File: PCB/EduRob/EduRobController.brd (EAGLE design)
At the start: 75 x 53.5 mm, 31 parts, among them J1 665306124022, J2 665306124022, M3 665306124022, M4 665306124022

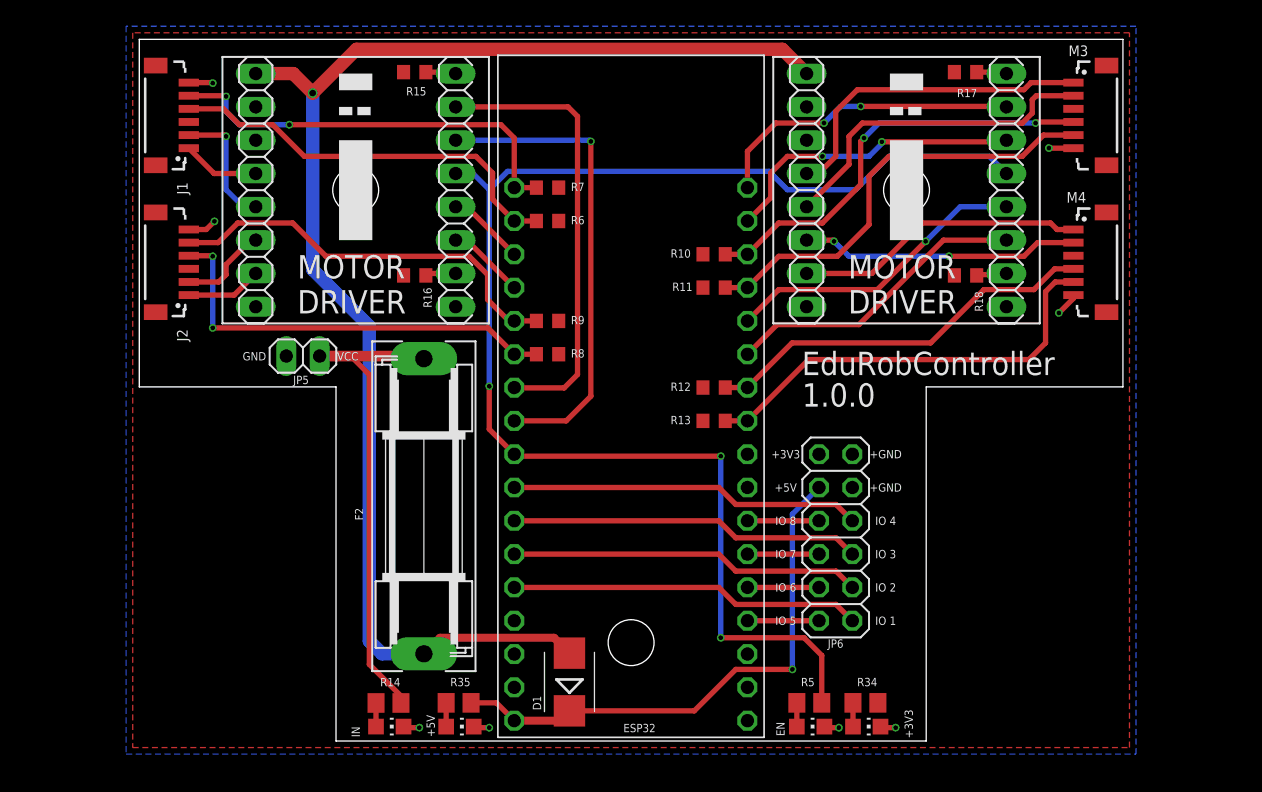
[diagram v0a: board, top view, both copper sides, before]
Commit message: New Connectors and minor changes
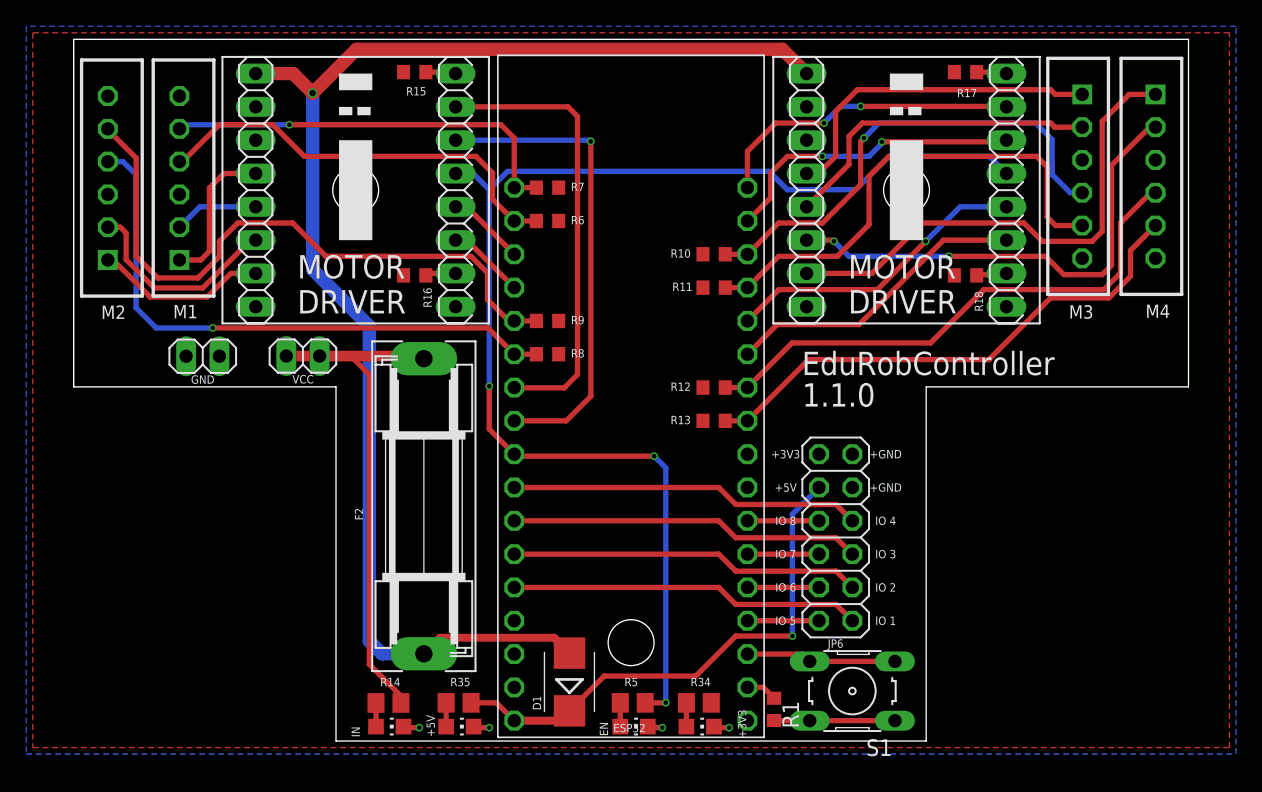
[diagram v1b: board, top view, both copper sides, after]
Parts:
- removed J1, J2, M3, M4: 665306124022, Wurth_Connectors_WR-WTB:665306124022
- added JP1: (no value), pinhead:1X02
- added P1, P2, P3, P4: B6B-EH-A, con-jst-eh:B6B-EH-A
- added R1: (no value), rcl:R0603
- added S1: (no value), switch-omron:B3F-10XX
- moved R5 13.5 mm to (22.6, 2.91)
- moved EN 13.5 mm to (22.7, 1.10)
- moved +3V3 12.7 mm to (27.8, 1.10)
- moved R34 12.7 mm to (27.7, 2.91)
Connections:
- new net N$2: R1.2, S1.1, S1.2
- net +3V3: now also P1.3, P2.3, P3.3, P4.3; no longer J1.3, J2.3, M3.3, M4.3
- net EN: now also S1.3, S1.4
- net GND: now also JP1.1, JP1.2, P1.6, P2.6, P3.6, P4.6, R1.1; no longer J1.6, J2.6, JP5.2, M3.6, M4.6
- net M1A: now also P1.1; no longer J1.1
- net M1B: now also P1.2; no longer J1.2
- net M1ENCA: now also P1.4; no longer J1.4
- net M1ENCB: now also P1.5; no longer J1.5
- net M2A: now also P2.1; no longer J2.1
- net M2B: now also P2.2; no longer J2.2
- net M2ENCA: now also P2.4; no longer J2.4
- net M2ENCB: now also P2.5; no longer J2.5
- net M3A: now also P3.1; no longer M3.1
- net M3B: now also P3.2; no longer M3.2
- net M3ENCA: now also P3.4; no longer M3.4
- net M3ENCB: now also P3.5; no longer M3.5
- net M4A: now also P4.1; no longer M4.1
- net M4B: now also P4.2; no longer M4.2
- net M4ENCA: now also P4.4; no longer M4.4
- net M4ENCB: now also P4.5; no longer M4.5
- net VCC: now also JP5.2
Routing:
- net M2ENCB: track 31.3 -> 48.5 mm
- net M4A: track 22.1 -> 38.3 mm
- net M4B: track 21.3 -> 36.8 mm
- net M2ENCA: track 32.8 -> 44.7 mm, vias 2 -> 1
- net EN: track 0.00 -> 11.5 mm
- net M4ENCA: track 30.3 -> 41.2 mm
- net ENM: track 107.7 -> 97.7 mm
- net N$2: track 0.00 -> 9.23 mm
- net M2B: track 6.87 -> 15.9 mm
- net M2A: track 5.79 -> 13.2 mm
- net M4ENCB: track 33.2 -> 40.1 mm
- net M1A: track 5.90 -> 11.4 mm
- net GND: track 12.6 -> 7.26 mm, vias 8 -> 4
- net M3ENCB: track 33.5 -> 37.9 mm
- net M3ENCA: track 32.7 -> 37.1 mm, vias 2 -> 1
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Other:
- board size 75 x 53.5 mm -> 85 x 53.5 mm
- board text added: "M1"
- board text added: "M2"
- board text added: "M3"
- board text added: "M4"
